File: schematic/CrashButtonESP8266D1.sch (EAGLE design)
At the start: 32 parts, among them U1 ESP12E_DEVKIT

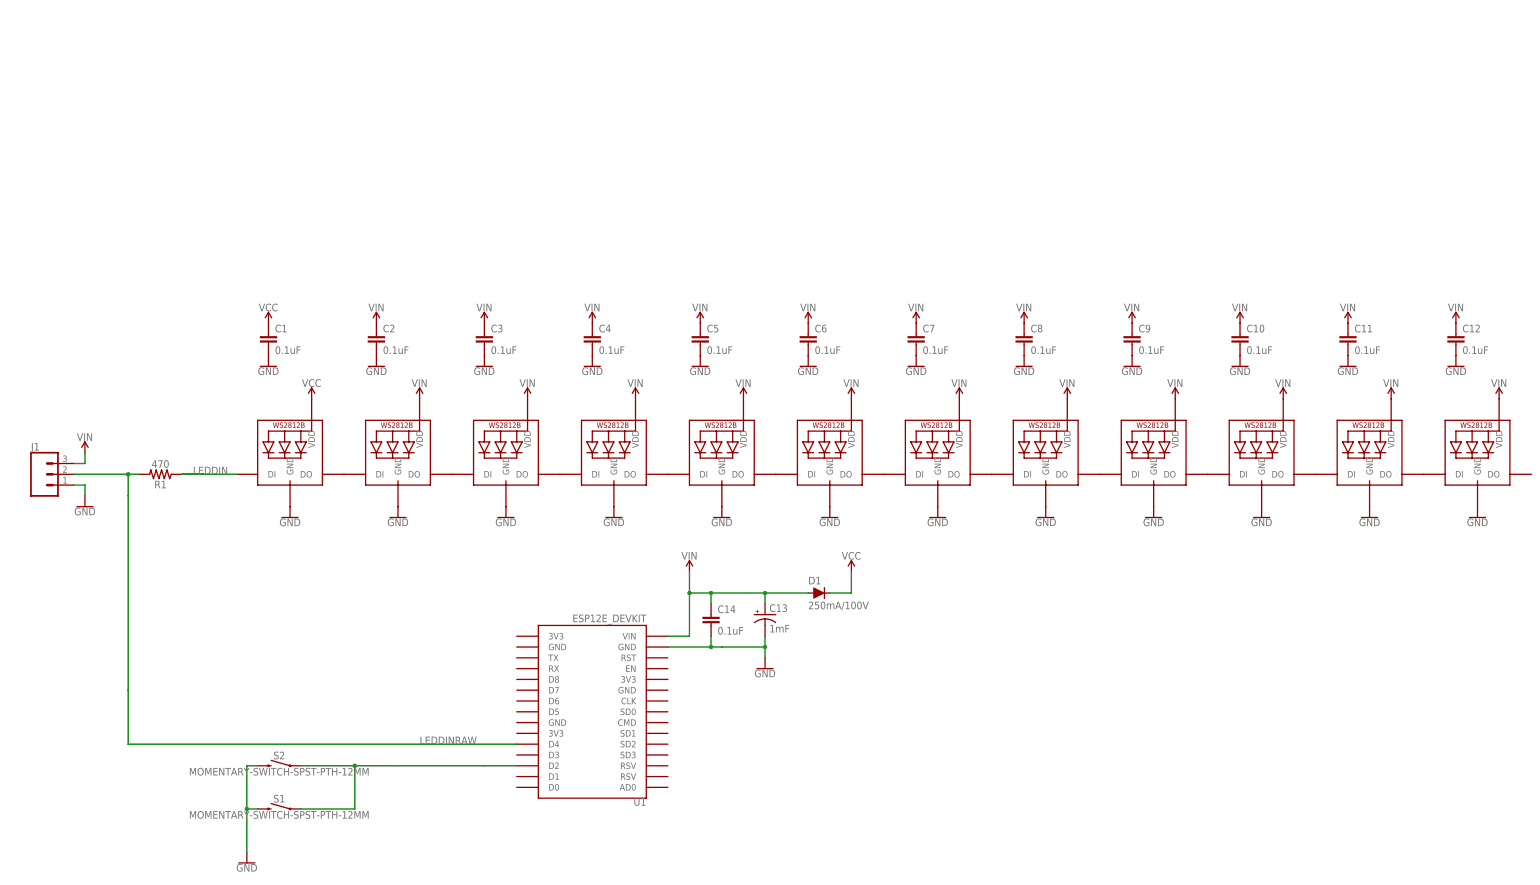
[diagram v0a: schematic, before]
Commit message: added board that uses D1 mini style esp8266
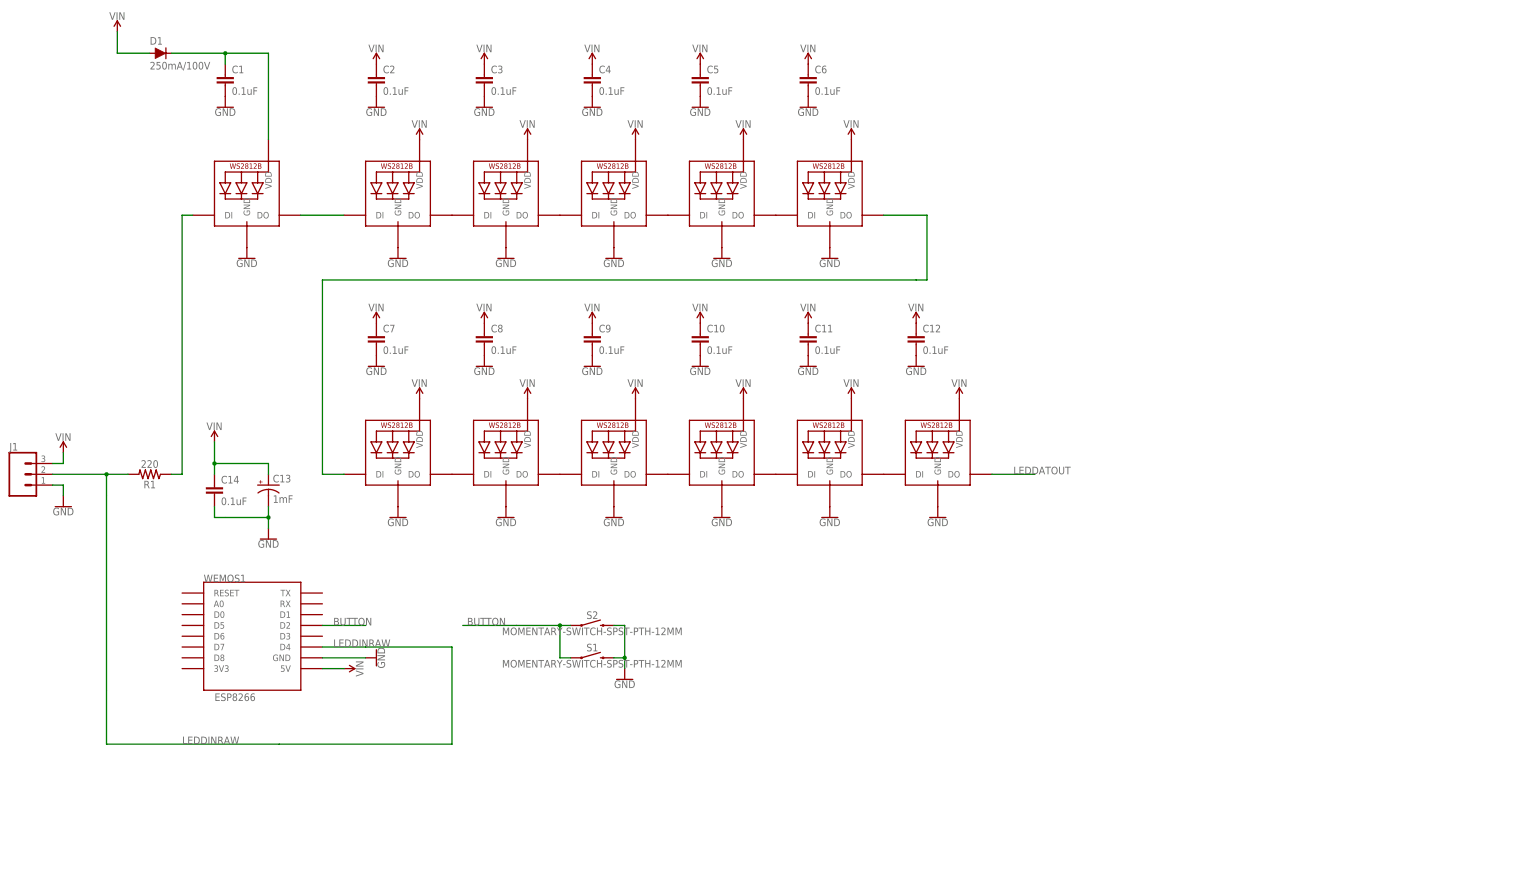
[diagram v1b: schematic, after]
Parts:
- removed U1: ESP12E_DEVKIT, ESP12E_DEVKIT:ESP12E_DEVKIT
- added WEMOS1: ESP8266, esp8266modules:WEMOS-D1-MINI
- R1: value 470 -> 220
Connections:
- net LEDDIN renamed N$10
- net VCC renamed N$11
- removed net N$10 (its old number): S1.1, S2.1, U1.D2
- new net BUTTON: S1.1, S2.1, WEMOS1.D2
- new net LEDDATOUT: LED12.DO
- net GND: now also WEMOS1.GND; no longer U1.GND@1
- net LEDDINRAW: now also WEMOS1.D4; no longer U1.D4
- net VIN: now also WEMOS1.5V; no longer U1.VIN
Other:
- moved on the sheet: C1, C10, C11, C12, C13, C14, C2, C3, C4, C5, C6, C7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

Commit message: schematic updates
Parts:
- added J2: (no value), SparkFun-Connectors:CONN_02
- added R2: 220, SparkFun-Resistors:470OHM-0603-1/10W-1%
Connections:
- new net N$14: R2.2, WEMOS1.D2
- net BUTTON: now also J2.1, R2.1; no longer WEMOS1.D2
- net GND: now also J2.2
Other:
- moved on the sheet: S1, S2
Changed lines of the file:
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@@
 <part name="SUPPLY1" library="SparkFun-PowerSymbols" deviceset="VIN" device=""/>
 <part name="FRAME1" library="SparkFun-Aesthetics" deviceset="FRAME-A4L" device=""/>
+<part name="R2" library="SparkFun-Resistors" deviceset="470OHM" device="-0603-1/10W-1%" value="220"/>
+<part name="GND29" library="SparkFun-PowerSymbols" deviceset="GND" device=""/>
+<part name="J2" library="SparkFun-Connectors" deviceset="CONN_02" device=""/>
 </parts>
 <sheets>
@@
 </plain>
 <instances>
-<instance part="S1" gate="G$1" x="99.06" y="35.56"/>
+<instance part="S1" gate="G$1" x="106.68" y="35.56"/>
 <instance part="LED1" gate="G$1" x="17.78" y="142.24"/>
 <instance part="LED2" gate="G$1" x="53.34" y="142.24"/>
@@
 <instance part="GND10" gate="1" x="129.54" y="68.58"/>
 <instance part="GND11" gate="1" x="154.94" y="68.58"/>
-<instance part="GND12" gate="1" x="106.68" y="30.48"/>
+<instance part="GND12" gate="1" x="114.3" y="30.48"/>
 <instance part="R1" gate="G$1" x="-5.08" y="78.74" rot="R180"/>
-<instance part="S2" gate="G$1" x="99.06" y="43.18"/>
+<instance part="S2" gate="G$1" x="106.68" y="43.18"/>
 <instance part="LED12" gate="G$1" x="180.34" y="81.28"/>
 <instance part="GND14" gate="1" x="180.34" y="68.58"/>
@@
 <instance part="GND13" gate="1" x="-25.4" y="71.12"/>
 <instance part="WEMOS1" gate="D1" x="17.78" y="40.64"/>
-<instance part="GND28" gate="1" x="48.26" y="35.56" rot="MR270"/>
-<instance part="SUPPLY28" gate="G$1" x="40.64" y="33.02" rot="R270"/>
+<instance part="GND28" gate="1" x="50.8" y="33.02" rot="MR0"/>
+<instance part="SUPPLY28" gate="G$1" x="45.72" y="22.86"/>
 <instance part="SUPPLY1" gate="G$1" x="-12.7" y="182.88"/>
 <instance part="FRAME1" gate="G$1" x="-43.18" y="10.16" smashed="yes">
@@
 <attribute name="DESIGNER" x="183.08" y="16.51" size="2.54" layer="94" font="vector"/>
 </instance>
+<instance part="R2" gate="G$1" x="66.04" y="43.18" rot="R180"/>
+<instance part="GND29" gate="1" x="134.62" y="45.72"/>
+<instance part="J2" gate="G$1" x="144.78" y="50.8" rot="R180"/>
 </instances>
 <busses>
@@
 <pinref part="S1" gate="G$1" pin="2"/>
 <pinref part="GND12" gate="1" pin="GND"/>
-<wire x1="104.14" y1="35.56" x2="106.68" y2="35.56" width="0.1524" layer="91"/>
-<wire x1="106.68" y1="35.56" x2="106.68" y2="33.02" width="0.1524" layer="91"/>
+<wire x1="111.76" y1="35.56" x2="114.3" y2="35.56" width="0.1524" layer="91"/>
+<wire x1="114.3" y1="35.56" x2="114.3" y2="33.02" width="0.1524" layer="91"/>
 <pinref part="S2" gate="G$1" pin="2"/>
-<wire x1="104.14" y1="43.18" x2="106.68" y2="43.18" width="0.1524" layer="91"/>
-<wire x1="106.68" y1="43.18" x2="106.68" y2="35.56" width="0.1524" layer="91"/>
-<junction x="106.68" y="35.56"/>
+<wire x1="111.76" y1="43.18" x2="114.3" y2="43.18" width="0.1524" layer="91"/>
+<wire x1="114.3" y1="43.18" x2="114.3" y2="35.56" width="0.1524" layer="91"/>
+<junction x="114.3" y="35.56"/>
 </segment>
 <segment>
@@
 <pinref part="WEMOS1" gate="D1" pin="GND"/>
 <pinref part="GND28" gate="1" pin="GND"/>
-<wire x1="45.72" y1="35.56" x2="35.56" y2="35.56" width="0.1524" layer="91"/>
-</segment>
-</net>
-<net name="BUTTON" class="0">
-<segment>
-<pinref part="S1" gate="G$1" pin="1"/>
-<wire x1="93.98" y1="35.56" x2="91.44" y2="35.56" width="0.1524" layer="91"/>
-<pinref part="S2" gate="G$1" pin="1"/>
-<wire x1="93.98" y1="43.18" x2="91.44" y2="43.18" width="0.1524" layer="91"/>
-<wire x1="91.44" y1="35.56" x2="91.44" y2="43.18" width="0.1524" layer="91"/>
-<wire x1="91.44" y1="43.18" x2="81.28" y2="43.18" width="0.1524" layer="91"/>
-<junction x="91.44" y="43.18"/>
-<wire x1="68.58" y1="43.18" x2="81.28" y2="43.18" width="0.1524" layer="91"/>
-<label x="78.74" y="43.18" size="1.778" layer="95" rot="MR0"/>
-</segment>
-<segment>
-<pinref part="WEMOS1" gate="D1" pin="D2"/>
-<wire x1="35.56" y1="43.18" x2="45.72" y2="43.18" width="0.1524" layer="91"/>
-<label x="38.1" y="43.18" size="1.778" layer="95"/>
+<wire x1="50.8" y1="35.56" x2="35.56" y2="35.56" width="0.1524" layer="91"/>
+</segment>
+<segment>
+<pinref part="GND29" gate="1" pin="GND"/>
+<pinref part="J2" gate="G$1" pin="2"/>
+<wire x1="137.16" y1="48.26" x2="134.62" y2="48.26" width="0.1524" layer="91"/>
 </segment>
 </net>
@@
 <pinref part="WEMOS1" gate="D1" pin="5V"/>
 <pinref part="SUPPLY28" gate="G$1" pin="VIN"/>
+<wire x1="45.72" y1="22.86" x2="45.72" y2="20.32" width="0.1524" layer="91"/>
+<wire x1="45.72" y1="20.32" x2="40.64" y2="20.32" width="0.1524" layer="91"/>
+<wire x1="40.64" y1="20.32" x2="40.64" y2="33.02" width="0.1524" layer="91"/>
 <wire x1="40.64" y1="33.02" x2="35.56" y2="33.02" width="0.1524" layer="91"/>
 </segment>
@@
 </segment>
 </net>
+<net name="BUTTON" class="0">
+<segment>
+<pinref part="R2" gate="G$1" pin="1"/>
+<pinref part="S2" gate="G$1" pin="1"/>
+<wire x1="71.12" y1="43.18" x2="86.36" y2="43.18" width="0.1524" layer="91"/>
+<wire x1="86.36" y1="43.18" x2="96.52" y2="43.18" width="0.1524" layer="91"/>
+<wire x1="96.52" y1="43.18" x2="101.6" y2="43.18" width="0.1524" layer="91"/>
+<wire x1="96.52" y1="43.18" x2="96.52" y2="35.56" width="0.1524" layer="91"/>
+<junction x="96.52" y="43.18"/>
+<pinref part="S1" gate="G$1" pin="1"/>
+<wire x1="96.52" y1="35.56" x2="101.6" y2="35.56" width="0.1524" layer="91"/>
+<label x="73.66" y="43.18" size="1.778" layer="95"/>
+<wire x1="137.16" y1="50.8" x2="86.36" y2="50.8" width="0.1524" layer="91"/>
+<wire x1="86.36" y1="50.8" x2="86.36" y2="43.18" width="0.1524" layer="91"/>
+<junction x="86.36" y="43.18"/>
+<pinref part="J2" gate="G$1" pin="1"/>
+</segment>
+</net>
+<net name="N$14" class="0">
+<segment>
+<pinref part="WEMOS1" gate="D1" pin="D2"/>
+<pinref part="R2" gate="G$1" pin="2"/>
+<wire x1="35.56" y1="43.18" x2="60.96" y2="43.18" width="0.1524" layer="91"/>
+</segment>
+</net>

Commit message: updated schematic
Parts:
- R2: value 220 -> 1k
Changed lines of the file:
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@@
 <part name="SUPPLY1" library="SparkFun-PowerSymbols" deviceset="VIN" device=""/>
 <part name="FRAME1" library="SparkFun-Aesthetics" deviceset="FRAME-A4L" device=""/>
-<part name="R2" library="SparkFun-Resistors" deviceset="470OHM" device="-0603-1/10W-1%" value="220"/>
+<part name="R2" library="SparkFun-Resistors" deviceset="470OHM" device="-0603-1/10W-1%" value="1k"/>
 <part name="GND29" library="SparkFun-PowerSymbols" deviceset="GND" device=""/>
 <part name="J2" library="SparkFun-Connectors" deviceset="CONN_02" device=""/>
